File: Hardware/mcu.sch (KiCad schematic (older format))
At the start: 32 parts, among them J4 Conn_01x04_Male, Q33 NX7002AK, SW21 SW_Push, SW22 SW_Push, U1 STM32F411RCT6, U5 USBUF, U6 LTV-357T, Y1 8MHz

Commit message: linked footprints with 3D models in project directory
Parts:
- R57, R58, R60, R61: value 220 -> 220R
- U1: symbol STM32F411RETx -> STM32F411RCTx
- U5: value USBUF -> USBUF02W6; Catalog link (none) -> http://uk.farnell.com/stmicroelectronics/usbuf02w6/filter-l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
- U6: value LTV-357T -> VO617A; Catalog link (none) -> https://eu.mouser.com/ProductDetail/Vishay-Semiconductors/V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
- Y1: Catalog link (none) -> https://eu.mouser.com/ProductDetail/?qs=NE97hfUNX0Ef9OqIOqO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
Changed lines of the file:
@@
 $EndDescr
 $Comp
-L STM32F411RETx U1
+L STM32F411RCTx U1
 U 1 1 5A206318
 P 8000 5050
@@
 P 14200 3850
 F 0 "U5" H 13950 4050 50  0000 C CNN
-F 1 "USBUF" H 13900 3550 50  0000 L CNN
+F 1 "USBUF02W6" H 13900 3550 50  0000 L CNN
 F 2 "project_library:SOT-363_SC-70-6" H 14200 3500 50  0001 C CNN
 F 3 "" H 14200 3850 50  0001 C CNN
+F 4 "http://uk.farnell.com/stmicroelectronics/usbuf02w6/filter-low-pass-1ghz-sot-323-6/dp/2341659" H 14200 3850 60  0001 C CNN "Catalog link"
 	1    14200 3850
 	1    0    0    -1
@@
 P 3100 7200
 F 0 "R57" H 3150 7250 50  0000 L CNN
-F 1 "220" H 3150 7150 50  0000 L CNN
+F 1 "220R" H 3150 7150 50  0000 L CNN
 F 2 "project_library:R_0603" H 3100 7200 50  0001 C CNN
 F 3 "" H 3100 7200 50  0001 C CNN
@@
 P 3100 7850
 F 0 "R58" V 3000 7800 50  0000 L CNN
-F 1 "220" V 3200 7850 50  0000 C CNN
+F 1 "220R" V 3200 7850 50  0000 C CNN
 F 2 "project_library:R_0603" H 3100 7850 50  0001 C CNN
 F 3 "" H 3100 7850 50  0001 C CNN
@@
 P 4200 9050
 F 0 "U6" H 3990 9240 50  0000 L CNN
-F 1 "LTV-357T" H 4000 8850 50  0000 L CNN
+F 1 "VO617A" H 4000 8850 50  0000 L CNN
 F 2 "project_library:DIP4-smd" H 4000 8850 50  0001 L CIN
 F 3 "" H 4200 9050 50  0001 L CNN
+F 4 "https://eu.mouser.com/ProductDetail/Vishay-Semiconductors/VO617A-8X017T?qs=%2fha2pyFaduga7JDI9Y4HlZSPCPCm8mReb3LRegGLigzOqtsvsZdCeQ%3d%3d" H 4200 9050 60  0001 C CNN "Catalog link"
 	1    4200 9050
 	1    0    0    -1
@@
 P 3100 8850
 F 0 "R61" V 3000 8850 50  0000 C CNN
-F 1 "220" V 3200 8850 50  0000 C CNN
+F 1 "220R" V 3200 8850 50  0000 C CNN
 F 2 "project_library:R_0603" H 3100 8850 50  0001 C CNN
 F 3 "" H 3100 8850 50  0001 C CNN
@@
 P 4600 8750
 F 0 "R60" H 4550 8700 50  0000 R CNN
-F 1 "220" H 4550 8800 50  0000 R CNN
+F 1 "220R" H 4550 8800 50  0000 R CNN
 F 2 "project_library:R_0603" H 4600 8750 50  0001 C CNN
 F 3 "" H 4600 8750 50  0001 C CNN
@@
 F 2 "project_library:Oscillator_SMD_EuroQuartz_XO53-4pin_5.0x3.2mm_HandSoldering" H 2350 4850 50  0001 C CNN
 F 3 "" H 2350 4850 50  0001 C CNN
+F 4 "https://eu.mouser.com/ProductDetail/?qs=NE97hfUNX0Ef9OqIOqO2cA%3D%3D" H 2350 4850 60  0001 C CNN "Catalog link"
 	1    2350 4850
 	1    0    0    -1

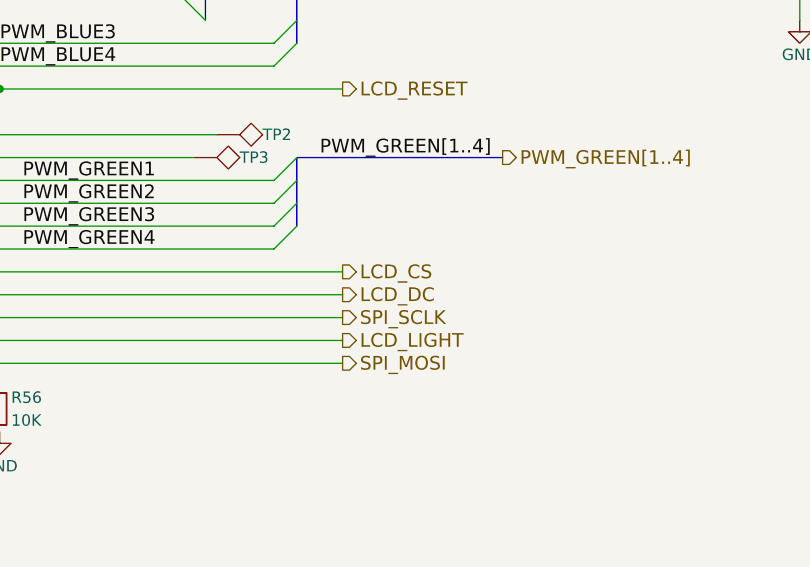
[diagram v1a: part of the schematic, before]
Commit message: changed pin of LCD CS, so hardware chip select could be used
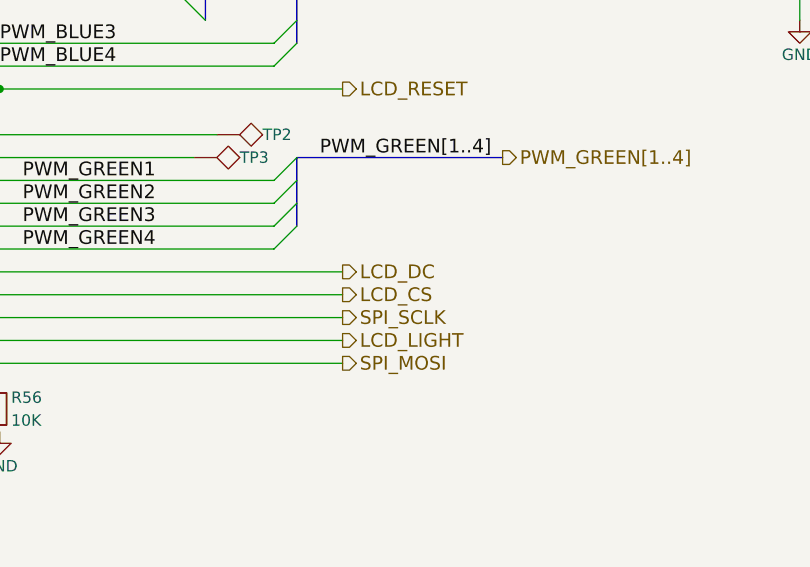
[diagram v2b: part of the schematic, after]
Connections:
- net LCD_CS: now also U1.33 (I2C2_SMBA/I2S2_WS/I2S3_CK/I2S4_WS/SPI2_NSS/SPI3_SCK/SPI4_NSS/TIM1_BKIN/PB12); no longer U1.29 (I2C2_SCL/I2S2_CK/I2S3_MCK/SDIO_D7/SPI2_SCK/TIM2_CH3/PB10)
- net LCD_DC: now also U1.29 (I2C2_SCL/I2S2_CK/I2S3_MCK/SDIO_D7/SPI2_SCK/TIM2_CH3/PB10); no longer U1.33 (I2C2_SMBA/I2S2_WS/I2S3_CK/I2S4_WS/SPI2_NSS/SPI3_SCK/SPI4_NSS/TIM1_BKIN/PB12)
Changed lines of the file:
@@
 Title "midi-grid"
 Date "2018-01-15"
-Rev "1.0"
+Rev "1.1"
 Comp ""
 Comment1 ""
@@
 Text HLabel 12500 6450 2    60   Output ~ 0
 LCD_LIGHT
+Text HLabel 12500 6150 2    60   Output ~ 0
+LCD_DC
 Text HLabel 12500 6250 2    60   Output ~ 0
-LCD_DC
-Text HLabel 12500 6150 2    60   Output ~ 0
 LCD_CS
 Text HLabel 12500 5350 2    60   Output ~ 0

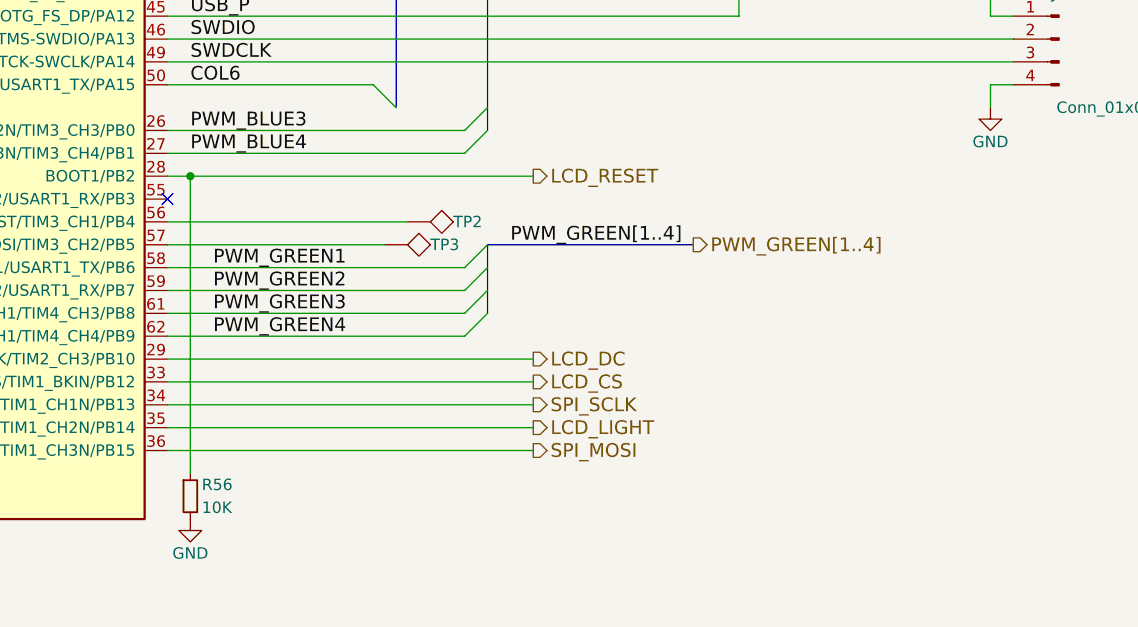
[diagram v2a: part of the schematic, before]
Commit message: rerouted LCD_LIGHT pin to PB5
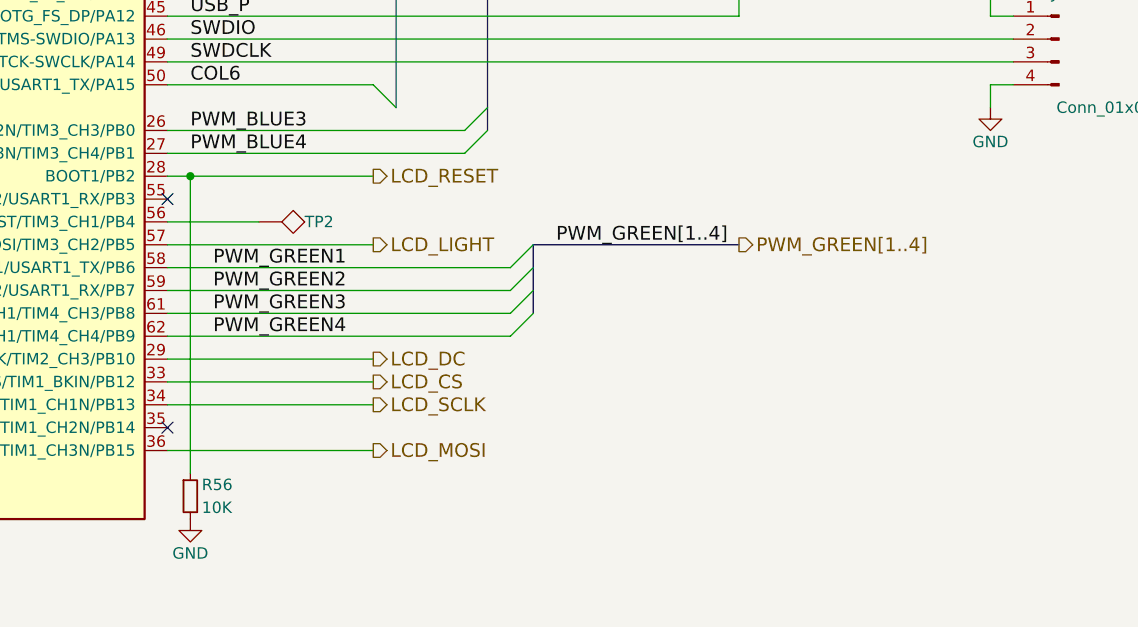
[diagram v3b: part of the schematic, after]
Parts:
- removed TP3: TEST, project_library:Test_Point_Pad_d3.0mm, symbol TEST
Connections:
- net LCD_LIGHT: now also U1.57 (I2C1_SMBA/I2S1_SD/I2S3_SD/SDIO_D3/SPI1_MOSI/SPI3_MOSI/TIM3_CH2/PB5); no longer U1.35 (I2S2_ext_SD/SDIO_D6/SPI2_MISO/TIM1_CH2N/PB14)
- net SPI_MOSI renamed LCD_MOSI
- net SPI_SCLK renamed LCD_SCLK
- no-connect marks 4 -> 5
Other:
- moved on the sheet: TP2
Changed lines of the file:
@@
 Entry Wire Line
 	12200 5250 12300 5150
-Text HLabel 13200 5650 2    60   Output ~ 0
+Text HLabel 13400 5650 2    60   Output ~ 0
 PWM_GREEN[1..4]
 Text Label 11000 4050 0    60   ~ 0
@@
 PWM_BLUE4
 Entry Wire Line
-	12200 5750 12300 5650
-Entry Wire Line
-	12200 5850 12300 5750
-Entry Wire Line
-	12200 5950 12300 5850
-Entry Wire Line
-	12200 6050 12300 5950
+	12400 5750 12500 5650
+Entry Wire Line
+	12400 5850 12500 5750
+Entry Wire Line
+	12400 5950 12500 5850
+Entry Wire Line
+	12400 6050 12500 5950
 Text HLabel 12500 3950 2    60   Output ~ 0
 PWM_BLUE[1..4]
@@
 	1    0    0    -1
 $EndComp
-Text HLabel 12500 6550 2    60   Output ~ 0
-SPI_MOSI
-Text HLabel 12500 6350 2    60   Output ~ 0
-SPI_SCLK
-Text HLabel 12500 6450 2    60   Output ~ 0
+Text HLabel 11800 6550 2    60   Output ~ 0
+LCD_MOSI
+Text HLabel 11800 6350 2    60   Output ~ 0
+LCD_SCLK
+Text HLabel 11800 5650 2    60   Output ~ 0
 LCD_LIGHT
-Text HLabel 12500 6150 2    60   Output ~ 0
+Text HLabel 11800 6150 2    60   Output ~ 0
 LCD_DC
-Text HLabel 12500 6250 2    60   Output ~ 0
+Text HLabel 11800 6250 2    60   Output ~ 0
 LCD_CS
-Text HLabel 12500 5350 2    60   Output ~ 0
+Text HLabel 11800 5350 2    60   Output ~ 0
 LCD_RESET
 Entry Wire Line
@@
 Text Label 12350 3350 0    60   ~ 0
 PWM_RED[1..4]
-Text Label 12400 5650 0    60   ~ 0
+Text Label 12600 5650 0    60   ~ 0
 PWM_GREEN[1..4]
 Text Label 12350 3950 0    60   ~ 0
@@
 L TEST TP2
 U 1 1 5A50623C
-P 11950 5550
-F 0 "TP2" V 11950 5750 50  0000 L CNN
-F 1 "TEST" V 11900 6000 50  0001 L CNN
-F 2 "project_library:Test_Point_Pad_d3.0mm" H 11950 5550 50  0001 C CNN
-F 3 "" H 11950 5550 50  0001 C CNN
-	1    11950 5550
-	0    1    1    0
-$EndComp
-$Comp
-L TEST TP3
-U 1 1 5A5062AA
-P 11850 5650
-F 0 "TP3" V 11850 5850 50  0000 L CNN
-F 1 "TEST" V 11800 6100 50  0001 L CNN
-F 2 "project_library:Test_Point_Pad_d3.0mm" H 11850 5650 50  0001 C CNN
-F 3 "" H 11850 5650 50  0001 C CNN
-	1    11850 5650
+P 11300 5550
+F 0 "TP2" V 11300 5750 50  0000 L CNN
+F 1 "TEST" V 11250 6000 50  0001 L CNN
+F 2 "project_library:Test_Point_Pad_d3.0mm" H 11300 5550 50  0001 C CNN
+F 3 "" H 11300 5550 50  0001 C CNN
+	1    11300 5550
 	0    1    1    0
 $EndComp
@@
 Connection ~ 11000 5350
 Wire Wire Line
-	10900 5350 12500 5350
+	10900 5350 11800 5350
 Wire Wire Line
 	11000 6650 11000 5350
@@
 	5100 5450 4800 5450
 Wire Wire Line
-	11850 5650 10900 5650
-Wire Wire Line
-	11950 5550 10900 5550
+	11800 5650 10900 5650
+Wire Wire Line
+	11300 5550 10900 5550
 Wire Wire Line
 	4800 5950 5100 5950
@@
 	2000 4550 5100 4550
 Wire Wire Line
-	10900 6550 12500 6550
-Wire Wire Line
-	10900 6450 12500 6450
-Wire Wire Line
-	10900 6350 12500 6350
-Wire Wire Line
-	10900 6250 12500 6250
-Wire Wire Line
-	12500 6150 10900 6150
+	10900 6550 11800 6550
+Wire Wire Line
+	10900 6350 11800 6350
+Wire Wire Line
+	10900 6250 11800 6250
+Wire Wire Line
+	11800 6150 10900 6150
 Wire Wire Line
 	10900 4950 11800 4950
@@
 	7800 6950 7800 7150
 Wire Bus Line
-	12300 5650 12300 5950
+	12500 5650 12500 5950
 Wire Bus Line
-	12300 5650 13200 5650
-Wire Wire Line
-	10900 6050 12200 6050
-Wire Wire Line
-	10900 5950 12200 5950
-Wire Wire Line
-	10900 5850 12200 5850
-Wire Wire Line
-	10900 5750 12200 5750
+	12500 5650 13400 5650
+Wire Wire Line
+	10900 6050 12400 6050
+Wire Wire Line
+	10900 5950 12400 5950
+Wire Wire Line
+	10900 5850 12400 5850
+Wire Wire Line
+	10900 5750 12400 5750
 Wire Wire Line
 	10900 5250 12200 5250
@@
 Wire Wire Line
 	10900 3450 12200 3450
+NoConn ~ 10900 6450
 $EndSCHEMATC

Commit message: converted all components except big tactile switches
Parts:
- C10, C11, C12, C13, C14, C15, C4, C5, C6, C7, C8, C9: symbol C_Small -> project_library:C_Small
- D158: symbol LL4148 -> project_library:LL4148
- J4: symbol Conn_01x04_Male -> project_library:Conn_01x04_Male
- Q33: symbol 2N7002 -> project_library:2N7002
- R55, R56, R57, R58, R59, R60, R61: symbol R_Small -> project_library:R_Small
- SW21, SW22: symbol SW_Push -> project_library:SW_Push
- TP1, TP2, TP4: symbol TEST -> project_library:TEST
- U1: symbol STM32F411RCTx -> project_library:STM32F411RCTx
- U5: symbol USBUF -> project_library:USBUF
- U6: symbol LTV-357T -> project_library:LTV-357T
- Y1: symbol Crystal_GND24 -> project_library:Crystal_GND24

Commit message: replaced all models with .step, deleted .wrl models
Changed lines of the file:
@@
 Connection ~ 11000 5350
 Wire Wire Line
-	10900 5350 11800 5350
+	10900 5350 11000 5350
 Wire Wire Line
 	11000 6650 11000 5350
@@
 	4600 8950 4600 8850
 Wire Wire Line
-	4500 8950 5000 8950
+	4500 8950 4600 8950
 Connection ~ 3400 9250
 Wire Wire Line
 	3400 9200 3400 9250
 Wire Wire Line
-	2800 9250 3800 9250
+	2800 9250 3400 9250
 Wire Wire Line
 	3800 9250 3800 9150
@@
 	3400 8850 3400 8900
 Wire Wire Line
-	3200 8850 3800 8850
+	3200 8850 3400 8850
 Wire Wire Line
 	2800 7850 3000 7850
@@
 	3800 8150 3800 8250
 Wire Wire Line
-	3700 8150 4900 8150
+	3700 8150 3800 8150
 Wire Wire Line
 	4400 4150 4400 3450
@@
 Connection ~ 2700 4850
 Wire Wire Line
-	2700 4650 2700 5050
+	2700 4650 2700 4850
 Wire Wire Line
 	2500 4850 2700 4850
@@
 	2200 4850 2000 4850
 Wire Wire Line
-	2000 4550 2000 5050
+	2000 4550 2000 4850
 Wire Wire Line
 	4800 2850 4800 2950
@@
 Connection ~ 4800 3650
 Wire Wire Line
-	4800 3350 4800 4150
+	4800 3350 4800 3650
 Wire Wire Line
 	5100 3650 4800 3650
@@
 Connection ~ 3200 3950
 Wire Wire Line
-	2800 3750 2800 4150
+	2800 3750 2800 3850
 Wire Wire Line
 	5100 3850 2800 3850
 Wire Wire Line
-	3200 3750 3200 4150
+	3200 3750 3200 3950
 Wire Wire Line
 	5100 3950 3200 3950
@@
 Wire Bus Line
 	11900 2750 12500 2750
-Wire Bus Line
-	11900 2750 11900 5050
 Wire Wire Line
 	11700 3350 11800 3350
@@
 Wire Wire Line
 	13400 4650 10900 4650
-Wire Bus Line
-	4100 4950 4100 5250
 Wire Bus Line
 	4100 4950 3800 4950
@@
 	7900 3050 7900 2850
 Wire Wire Line
-	7800 2650 7800 3050
+	7800 2650 7800 2850
 Connection ~ 8100 2850
 Wire Wire Line
@@
 	8100 2850 8000 2850
 Wire Wire Line
-	8100 2650 8100 3050
+	8100 2650 8100 2850
 Connection ~ 8200 7050
 Wire Wire Line
 	8100 7050 8200 7050
 Wire Wire Line
-	8200 6950 8200 7150
+	8200 6950 8200 7050
 Wire Wire Line
 	8100 6950 8100 7050
@@
 	7800 7050 7900 7050
 Wire Wire Line
-	7800 6950 7800 7150
-Wire Bus Line
-	12500 5650 12500 5950
+	7800 6950 7800 7050
 Wire Bus Line
 	12500 5650 13400 5650
@@
 	10900 5150 12200 5150
 Wire Bus Line
-	12300 3950 12300 5150
-Wire Bus Line
 	12300 3950 12500 3950
 Wire Wire Line
@@
 Wire Wire Line
 	10900 4050 12200 4050
-Wire Bus Line
-	12300 3350 12300 3650
 Wire Bus Line
 	12300 3350 13050 3350
@@
 	10900 3450 12200 3450
 NoConn ~ 10900 6450
+Wire Wire Line
+	11000 5350 11800 5350
+Wire Wire Line
+	4600 8950 5000 8950
+Wire Wire Line
+	3400 9250 3800 9250
+Wire Wire Line
+	3400 8850 3800 8850
+Wire Wire Line
+	3800 8150 4900 8150
+Wire Wire Line
+	2700 4850 2700 5050
+Wire Wire Line
+	2000 4850 2000 5050
+Wire Wire Line
+	4800 3650 4800 4150
+Wire Wire Line
+	2800 3850 2800 4150
+Wire Wire Line
+	3200 3950 3200 4150
+Wire Wire Line
+	7800 2850 7800 3050
+Wire Wire Line
+	8100 2850 8100 3050
+Wire Wire Line
+	8200 7050 8200 7150
+Wire Wire Line
+	7800 7050 7800 7150
+Wire Bus Line
+	12300 3350 12300 3650
+Wire Bus Line
+	12300 3950 12300 5150
+Wire Bus Line
+	12500 5650 12500 5950
+Wire Bus Line
+	4100 4950 4100 5250
+Wire Bus Line
+	11900 2750 11900 5050
 $EndSCHEMATC

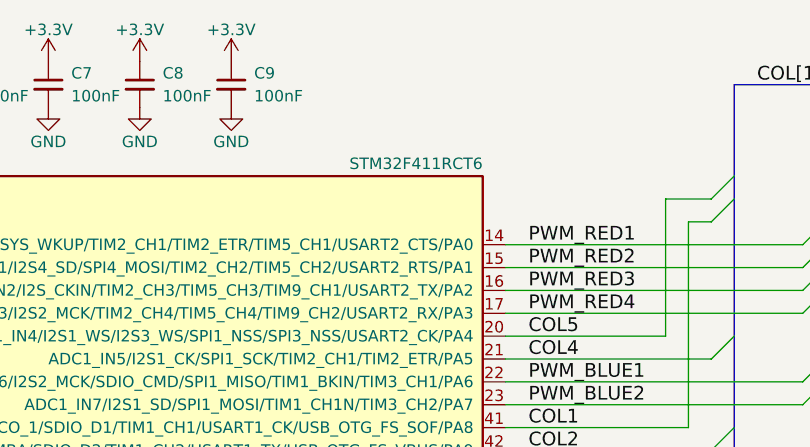
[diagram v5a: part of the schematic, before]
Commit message: renamed Image class to ImageMono, replaced microcontroller with STM32F413RH
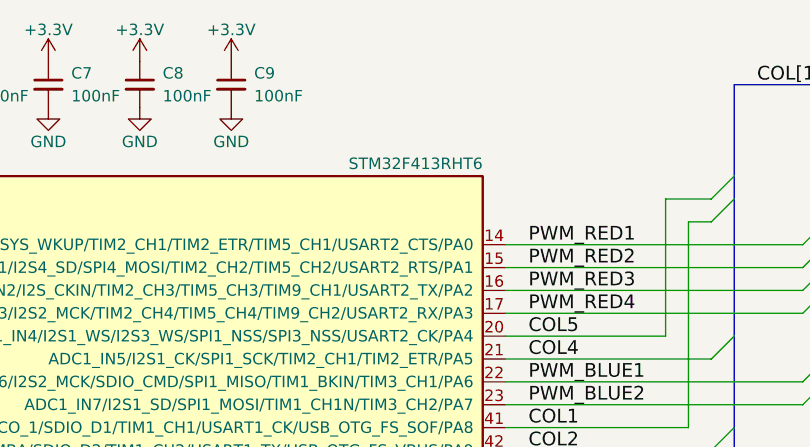
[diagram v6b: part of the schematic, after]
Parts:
- U1: value STM32F411RCT6 -> STM32F413RHT6
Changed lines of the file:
@@
 EESchema Schematic File Version 4
-LIBS:midi_grid-cache
 EELAYER 30 0
 EELAYER END
@@
 P 8000 5050
 F 0 "U1" H 5200 6975 50  0000 L BNN
-F 1 "STM32F411RCT6" H 10800 6975 50  0000 R BNN
+F 1 "STM32F413RHT6" H 10800 6975 50  0000 R BNN
 F 2 "project_library:LQFP-64_10x10mm_Pitch0.5mm" H 10800 6925 50  0001 R TNN
 F 3 "" H 8000 5050 50  0001 C CNN
